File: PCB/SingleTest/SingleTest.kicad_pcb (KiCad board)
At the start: 2 copper layers, 62 x 63 mm, 14 parts, among them J1 Conn_01x08

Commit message: Adding labels
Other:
- board text added: "C"
- board text added: "C0"
- board text added: "C1"
- board text added: "D"
- board text added: "G"
- board text added: "R0"
- board text added: "R1"
- board text added: "V"
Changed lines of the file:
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@@
     (links 24)
     (no_connects 1)
-    (area 82.924999 82.924999 145.075001 145.075001)
+    (area 82.924999 82.924999 145.075001 146.075001)
     (thickness 1.6)
-    (drawings 4)
+    (drawings 12)
     (tracks 76)
     (zones 0)
@@
     (45 Margin user)
     (46 B.CrtYd user)
-    (47 F.CrtYd user)
+    (47 F.CrtYd user hide)
     (48 B.Fab user)
     (49 F.Fab user hide)
@@
     (pad "" thru_hole rect (at -7.5 7.6 90) (size 1.6 1.6) (drill 0.8) (layers *.Cu *.Mask))
   )
+  (gr_text R0 (at 91 84) (layer B.SilkS)
+    (effects (font (size 1 1) (thickness 0.25)) (justify mirror))
+  )
+  (gr_text G (at 108.8 84) (layer B.SilkS)
+    (effects (font (size 1 1) (thickness 0.25)) (justify mirror))
+  )
+  (gr_text D (at 106.2 84) (layer B.SilkS)
+    (effects (font (size 1 1) (thickness 0.25)) (justify mirror))
+  )
+  (gr_text C (at 103.6 84) (layer B.SilkS)
+    (effects (font (size 1 1) (thickness 0.25)) (justify mirror))
+  )
+  (gr_text V (at 101.2 84) (layer B.SilkS)
+    (effects (font (size 1 1) (thickness 0.25)) (justify mirror))
+  )
+  (gr_text C1 (at 98.5 84) (layer B.SilkS)
+    (effects (font (size 1 1) (thickness 0.25)) (justify mirror))
+  )
+  (gr_text C0 (at 96 84) (layer B.SilkS)
+    (effects (font (size 1 1) (thickness 0.25)) (justify mirror))
+  )
+  (gr_text R1 (at 93.5 84) (layer B.SilkS)
+    (effects (font (size 1 1) (thickness 0.25)) (justify mirror))
+  )
   (gr_line (start 83 83) (end 145 83) (angle 90) (layer Edge.Cuts) (width 0.15))

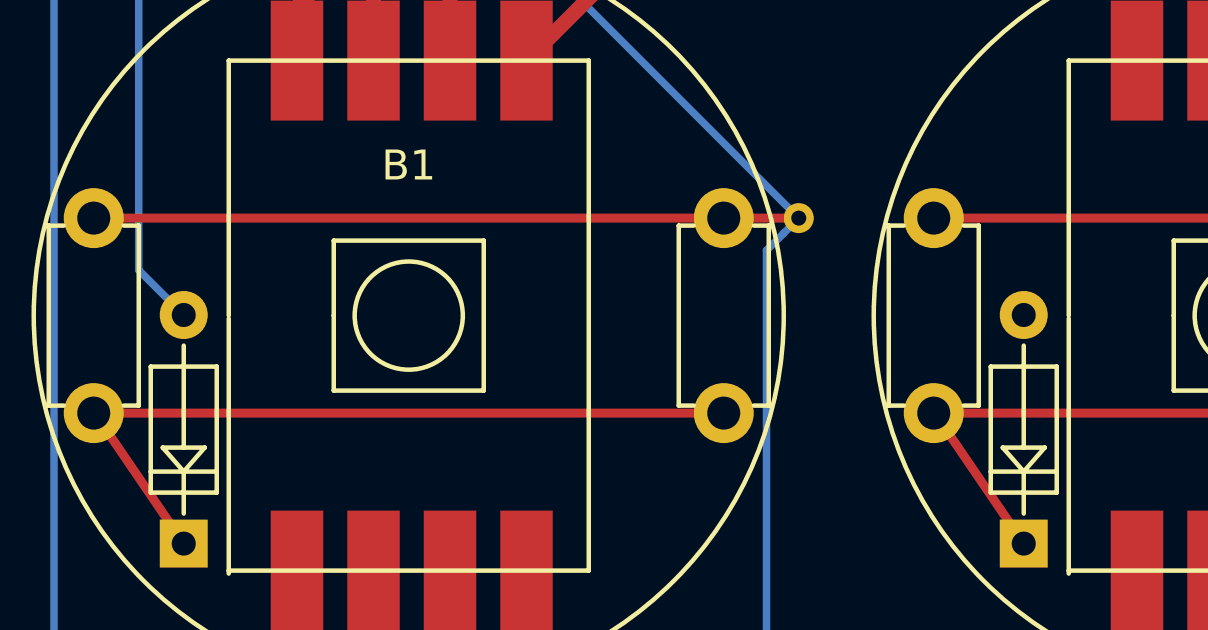
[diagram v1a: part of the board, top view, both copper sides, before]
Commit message: fix row0
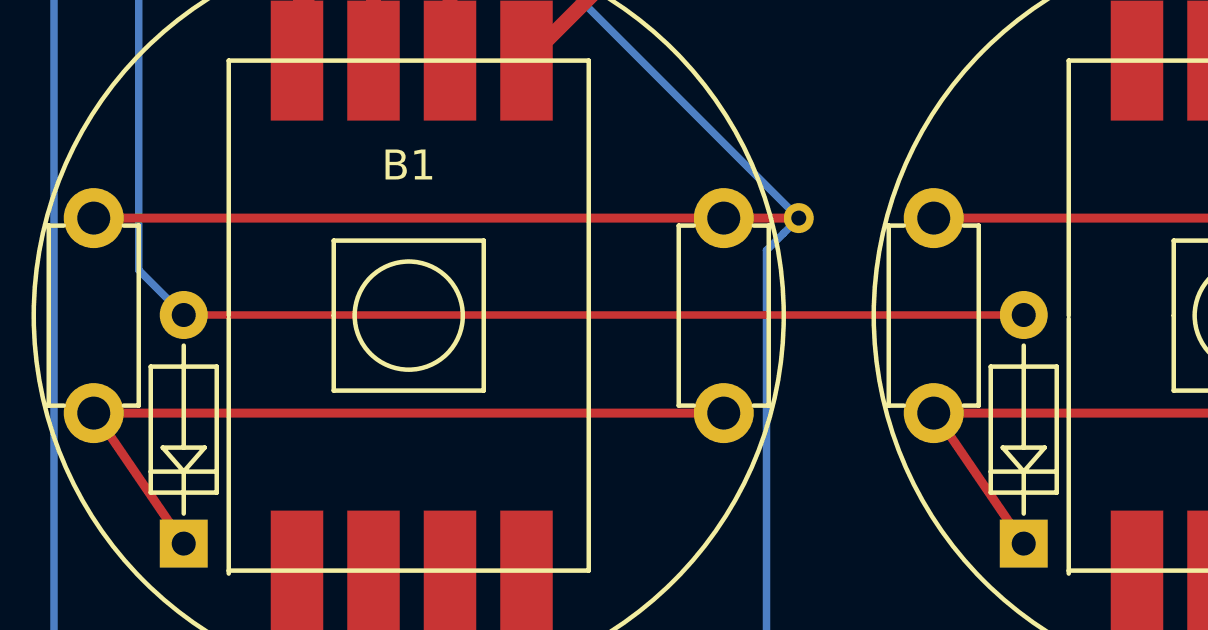
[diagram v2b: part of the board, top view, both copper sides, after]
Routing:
- net ROW_0: track 15.1 -> 43.1 mm
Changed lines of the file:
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@@
   (general
     (links 24)
-    (no_connects 1)
+    (no_connects 0)
     (area 82.924999 82.924999 145.075001 146.075001)
     (thickness 1.6)
     (drawings 12)
-    (tracks 76)
+    (tracks 77)
     (zones 0)
     (modules 14)
@@
     (45 Margin user)
     (46 B.CrtYd user)
-    (47 F.CrtYd user hide)
+    (47 F.CrtYd user)
     (48 B.Fab user)
     (49 F.Fab user hide)
@@
   (segment (start 111.924999 123.674999) (end 111.924999 97.825001) (width 0.25) (layer B.Cu) (net 1))
   (segment (start 111.924999 97.825001) (end 112.500001 97.249999) (width 0.25) (layer B.Cu) (net 1))
+  (segment (start 92.5 99.98) (end 120.5 99.98) (width 0.25) (layer F.Cu) (net 2) (status C00000))
   (segment (start 92.5 99.98) (end 91 98.48) (width 0.25) (layer B.Cu) (net 2))
   (segment (start 91 98.48) (end 91 85.5) (width 0.25) (layer B.Cu) (net 2))
